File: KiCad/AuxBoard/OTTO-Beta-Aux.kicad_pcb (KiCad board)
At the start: 2 copper layers, 288.5 x 95 mm, 212 parts, among them J1 Conn_01x20, J1_KD028QVFMA17 Conn_02x25_Counter_Clockwise, Q1 AO3400A, SW1 ALPS SKHC, SW10 ALPS SKHC, SW11 ALPS SKHC, SW12 ALPS SKHC, SW13 ALPS SKHC, SW14 ALPS SKHC, SW15 ALPS SKHC, SW16 ALPS SKHC, SW17 ALPS SKHC, SW18 ALPS SKHC, SW19 ALPS SKHC, SW2 ALPS SKHC, SW20 ALPS SKHC, SW21 ALPS SKHC, SW22 ALPS SKHC, SW23 ALPS SKHC, SW24 ALPS SKHC, SW25 ALPS SKHC, SW26 ALPS SKHC, SW27 6x6x13mm, SW28 6x6x13mm, SW29 6x6x13mm, SW3 ALPS SKHC, SW30 6x6x13mm, SW31 6x6x13mm, SW32 6x6x13mm, SW33 6x6x13mm, SW34 6x6x13mm, SW35 6x6x13mm, SW36 6x6x13mm, SW37 6x6x13mm, SW38 6x6x13mm, SW39 6x6x13mm, SW4 ALPS SKHC, SW40 6x6x13mm, SW41 6x6x13mm, SW42 6x6x13mm, SW43 6x6x13mm, SW44 6x6x13mm, SW45 6x6x13mm, SW46 6x6x13mm, SW47 6x6x13mm, SW5 ALPS SKHC, SW50 6x6x13mm, SW51 6x6x13mm, SW52 6x6x13mm, SW53 6x6x13mm, SW54 6x6x13mm, SW55 6x6x13mm, SW56 6x6x13mm, SW6 ALPS SKHC, SW7 ALPS SKHC, SW8 ALPS SKHC, SW9 ALPS SKHC, U1 SN74LV1T34_SOT-23_A, U2 TPS22918_SOT23-6_A

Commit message: Smaller Aux board
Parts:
- removed H3, H4, H5: MountingHole_Pad, OTTO_Footprints_Lib:MountingHoleHole
- removed SW1, SW10, SW11, SW12, SW13, SW14, SW15, SW16, SW2, SW3, SW4, SW5, SW6, SW7, SW8, SW9: ALPS SKHC, OTTO_Footprints_Lib:ALPS_SKHC_aux_hole
- moved FID10 21.2 mm to (153.6, 77.7)
- moved FID4 21.2 mm to (153.6, 77.7)
- moved H102 20.2 mm to (20.2, 86.1)
- moved FID2 14.9 mm to (24.4, 74.2)
- moved FID8 14.9 mm to (24.4, 74.2)
- moved FID12 13.9 mm to (282.2, 80.7)
- moved FID6 13.9 mm to (282.2, 80.7)
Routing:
- net Net-(LED8-Pad2): track 18.7 -> 25.7 mm
- net +5V_LEDS: track 1374.1 -> 1379.5 mm, vias 57 -> 56
- net Net-(LED1-Pad2): track 18.5 -> 16.5 mm
- net GND: vias 119 -> 114
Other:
- board size 288.5 x 95 mm -> 288.5 x 80.1 mm

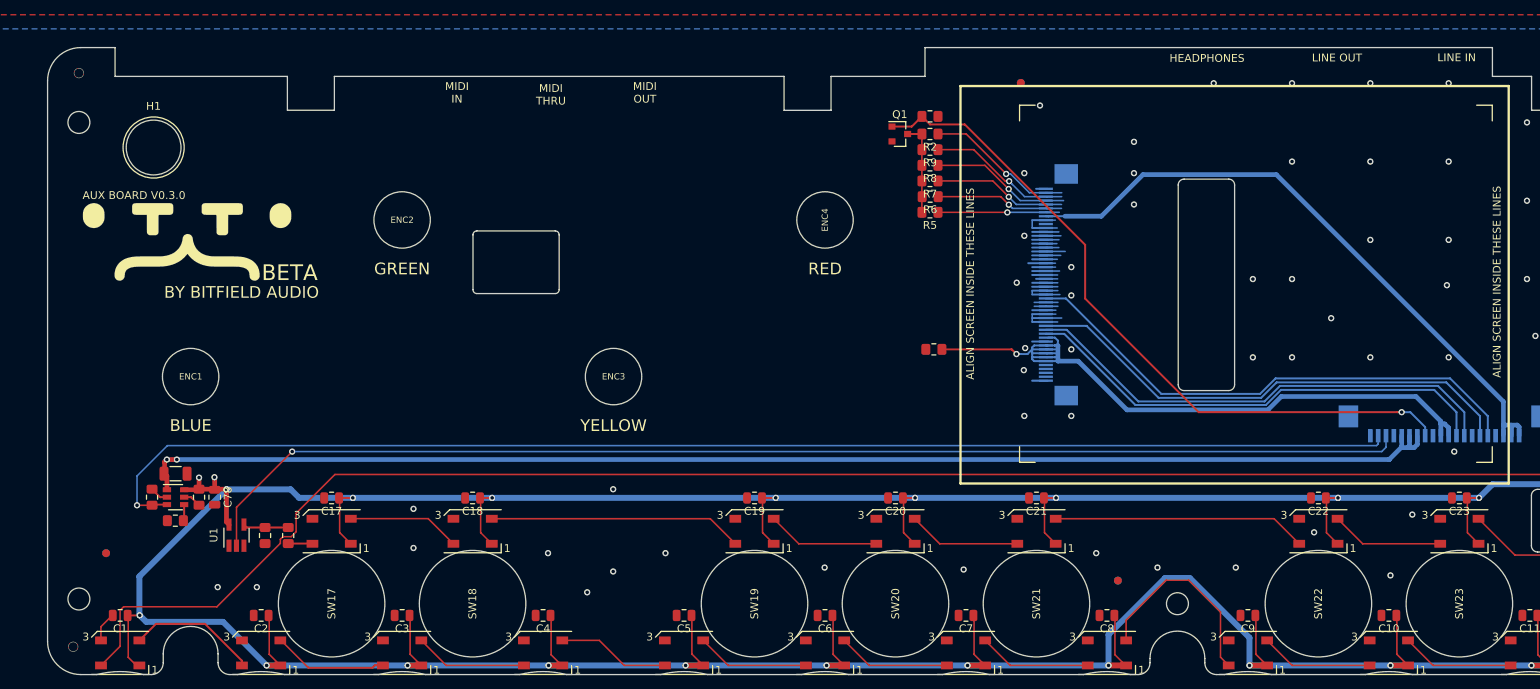
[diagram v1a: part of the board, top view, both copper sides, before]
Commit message: Aux v0.3.0
Small adjustments to PCB outline
switch to WS2812C LEDs
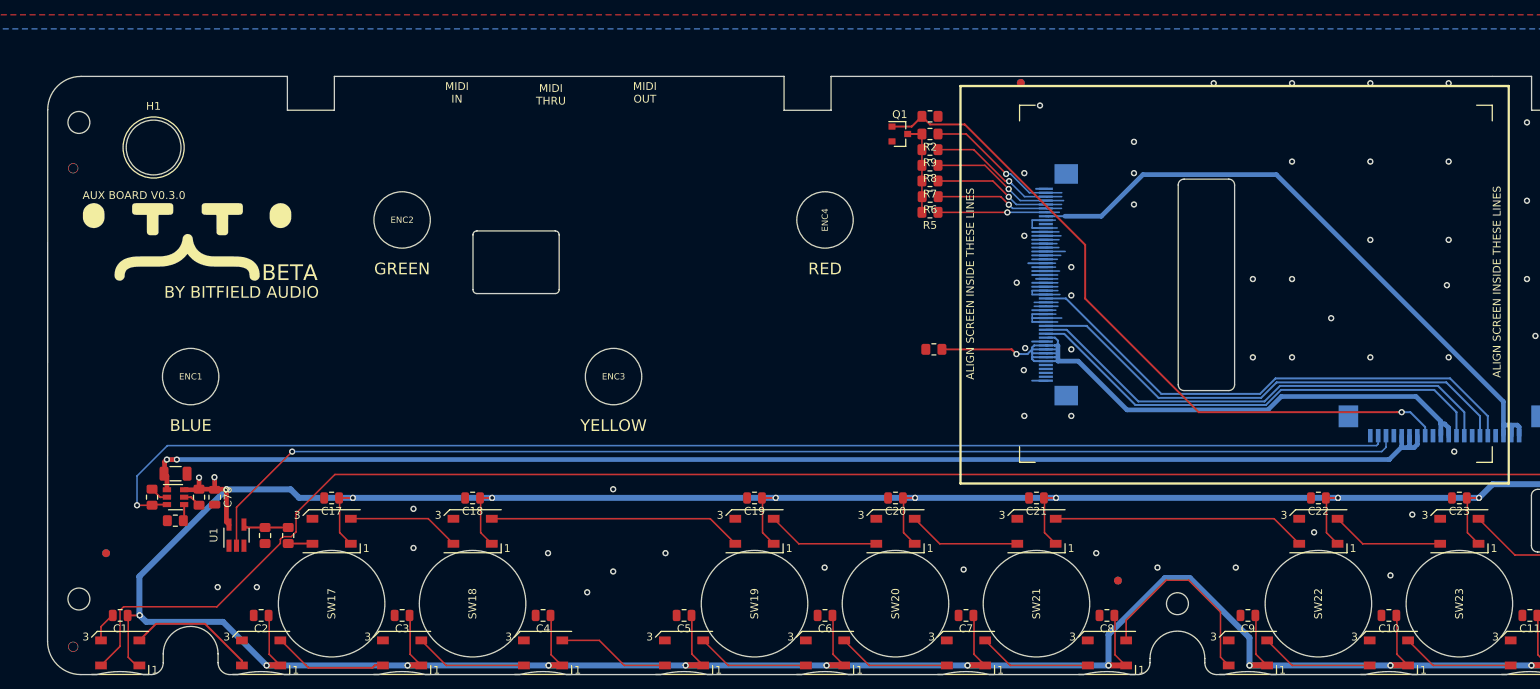
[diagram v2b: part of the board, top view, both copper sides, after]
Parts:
- ENC1, ENC2, ENC3, ENC4: value ALPS EC11E183440C -> ALPS EC11 HOLE
- LED1, LED10, LED11, LED12, LED13, LED14, LED15, LED16, LED17, LED18, LED19, LED2, LED20, LED21, LED22, LED23, LED24, LED25, LED26, LED27, LED28, LED29, LED3, LED30, LED31, LED32, LED33, LED34, LED35, LED36, LED37, LED38, LED39, LED4, LED40, LED41, LED42, LED43, LED44, LED45, LED46, LED47, LED48, LED49, LED5, LED50, LED51, LED52, LED53, LED54, LED6, LED7, LED8, LED9: value WS2812B -> WS2812C
- SW17, SW18, SW19, SW20, SW21, SW22, SW23, SW24, SW25, SW26: value ALPS SKHC -> ALPS SKHC Hole
- SW27, SW28, SW29, SW30, SW31, SW32, SW33, SW34, SW35, SW36, SW37, SW38, SW39, SW40, SW41, SW42, SW43, SW44, SW45, SW46, SW47, SW50, SW51, SW52, SW53, SW54, SW55, SW56: value 6x6x13mm -> 6x6x13mm Hole
- moved H101 12.2 mm to (20.2, 25.0)
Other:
- outline, holes or cut-outs redrawn
- board text removed: "HEADPHONES"
- board text removed: "LINE IN"
- board text removed: "LINE OUT"

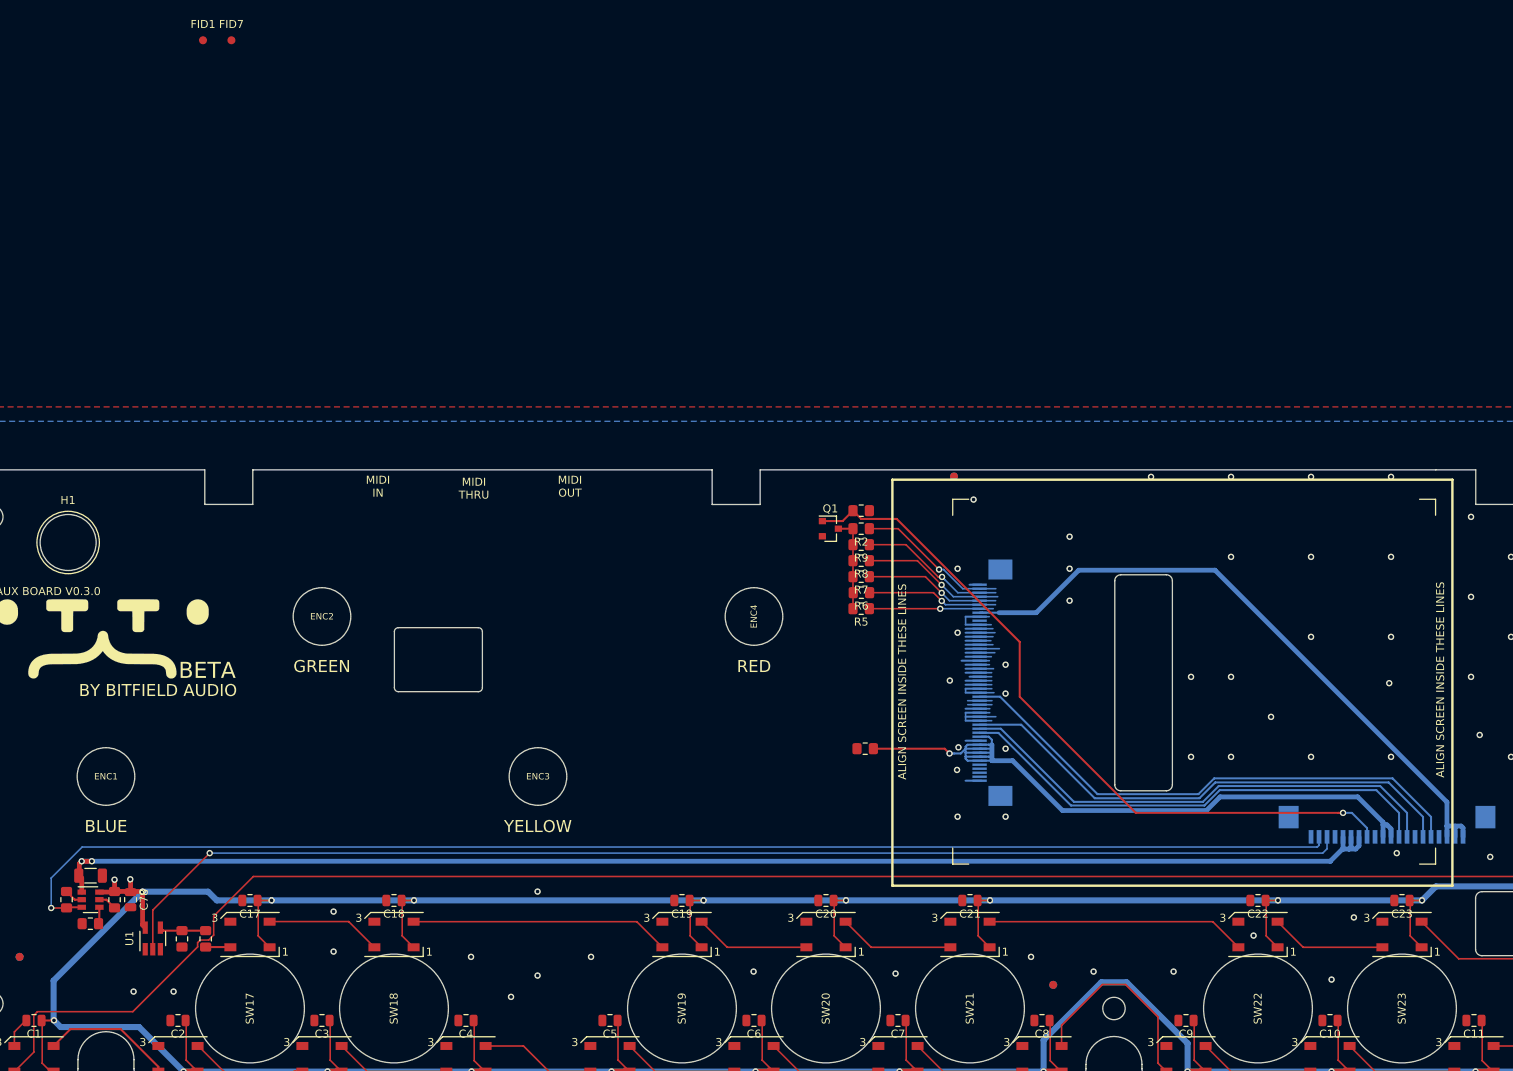
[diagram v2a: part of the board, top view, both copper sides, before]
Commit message: Put LEDs on RPI power rail on aux board
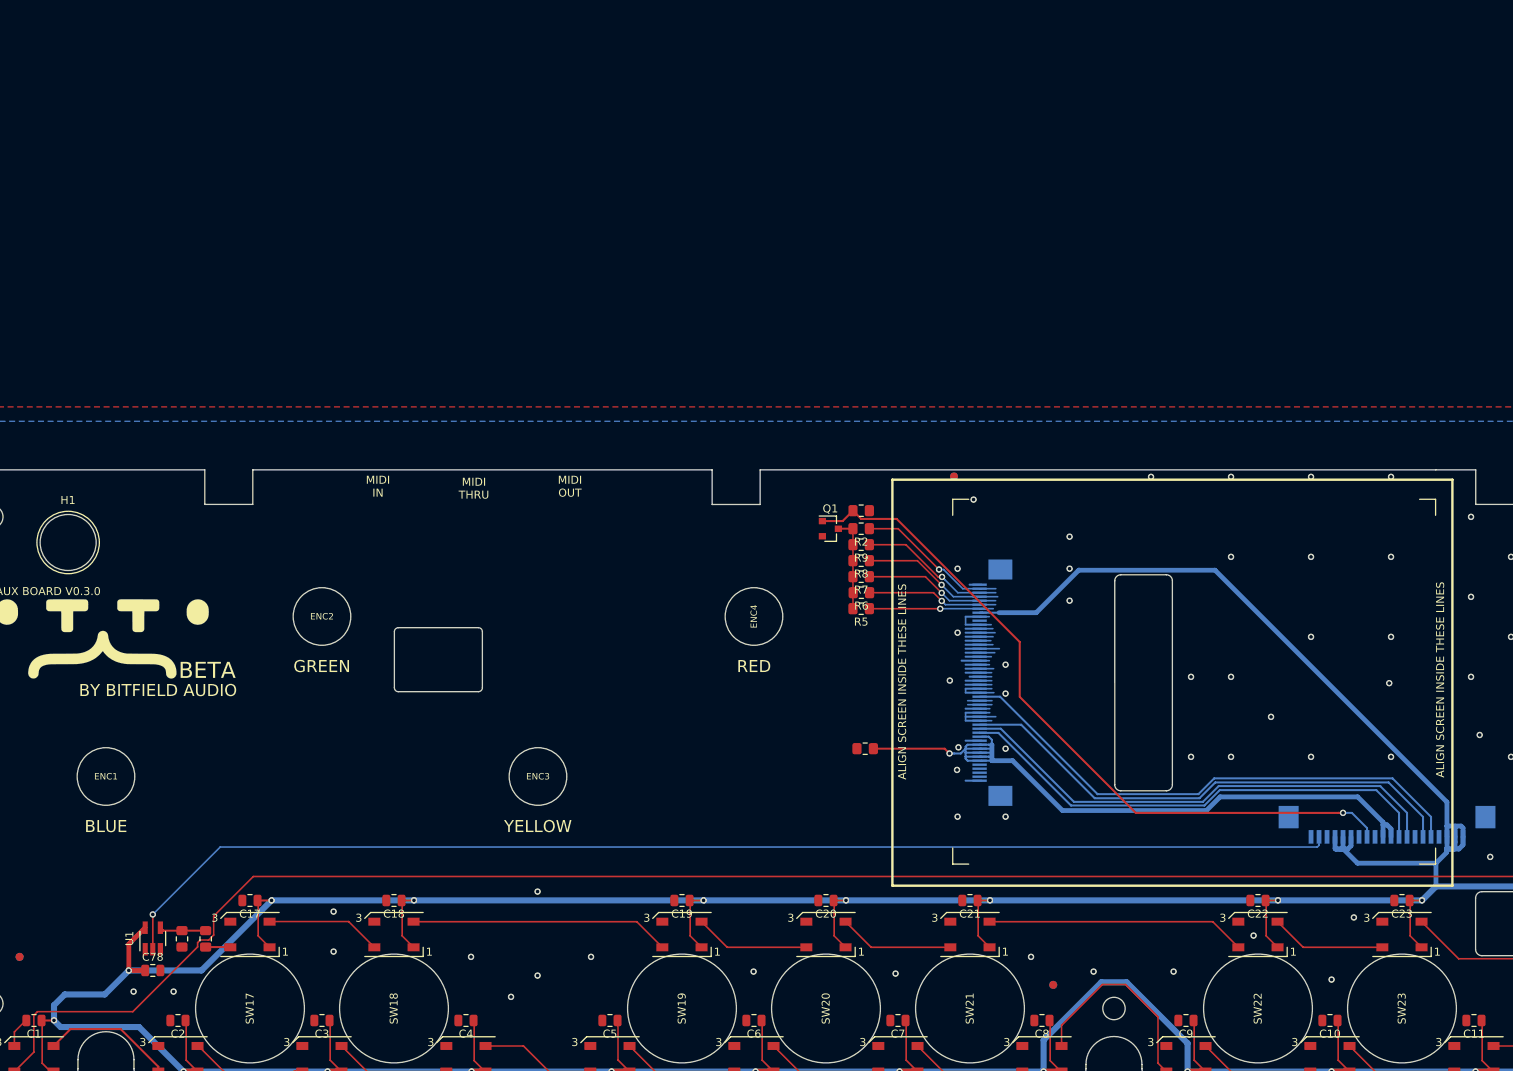
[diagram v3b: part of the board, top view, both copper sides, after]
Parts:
- removed C49: 47uF, Capacitor_SMD:C_1206_3216Metric
- removed C50: 10nF, Capacitor_SMD:C_0805_2012Metric_Pad1.15x1.40mm_HandSolder
- removed FID1, FID7: Fiducial, Fiducial:Fiducial_1mm_Mask2mm
- removed R3: 100k, Resistor_SMD:R_0805_2012Metric_Pad1.15x1.40mm_HandSolder
- removed R4: 0, Resistor_SMD:R_0805_2012Metric_Pad1.15x1.40mm_HandSolder
- removed U2: TPS22918_SOT23-6_A, OTTO_Footprints_Lib:SOT-23-6
- moved C78 9.27 mm to (41.1, 75.8), turned to 0 degrees
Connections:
- C1 pad 1: +5V_LEDS -> +5V
- C10 pad 1: +5V_LEDS -> +5V
- C100 pad 1: +5V_LEDS -> +5V
- C101 pad 1: +5V_LEDS -> +5V
- C102 pad 1: +5V_LEDS -> +5V
- C103 pad 1: +5V_LEDS -> +5V
- C104 pad 1: +5V_LEDS -> +5V
- C105 pad 1: +5V_LEDS -> +5V
- C11 pad 1: +5V_LEDS -> +5V
- C12 pad 1: +5V_LEDS -> +5V
- C13 pad 1: +5V_LEDS -> +5V
- C14 pad 1: +5V_LEDS -> +5V
- C15 pad 1: +5V_LEDS -> +5V
- C16 pad 1: +5V_LEDS -> +5V
- C17 pad 1: +5V_LEDS -> +5V
- C18 pad 1: +5V_LEDS -> +5V
- C19 pad 1: +5V_LEDS -> +5V
- C2 pad 1: +5V_LEDS -> +5V
- C20 pad 1: +5V_LEDS -> +5V
- C21 pad 1: +5V_LEDS -> +5V
- C22 pad 1: +5V_LEDS -> +5V
- C23 pad 1: +5V_LEDS -> +5V
- C24 pad 1: +5V_LEDS -> +5V
- C25 pad 1: +5V_LEDS -> +5V
- C26 pad 1: +5V_LEDS -> +5V
- C27 pad 1: +5V_LEDS -> +5V
- C28 pad 1: +5V_LEDS -> +5V
- C29 pad 1: +5V_LEDS -> +5V
- C3 pad 1: +5V_LEDS -> +5V
- C30 pad 1: +5V_LEDS -> +5V
- C31 pad 1: +5V_LEDS -> +5V
- C32 pad 1: +5V_LEDS -> +5V
- C33 pad 1: +5V_LEDS -> +5V
- C34 pad 1: +5V_LEDS -> +5V
- C35 pad 1: +5V_LEDS -> +5V
- C36 pad 1: +5V_LEDS -> +5V
- C37 pad 1: +5V_LEDS -> +5V
- C38 pad 1: +5V_LEDS -> +5V
- C39 pad 1: +5V_LEDS -> +5V
- C4 pad 1: +5V_LEDS -> +5V
- C40 pad 1: +5V_LEDS -> +5V
- C41 pad 1: +5V_LEDS -> +5V
- C42 pad 1: +5V_LEDS -> +5V
- C43 pad 1: +5V_LEDS -> +5V
- C44 pad 1: +5V_LEDS -> +5V
- C45 pad 1: +5V_LEDS -> +5V
- C46 pad 1: +5V_LEDS -> +5V
- C47 pad 1: +5V_LEDS -> +5V
- C5 pad 1: +5V_LEDS -> +5V
- C6 pad 1: +5V_LEDS -> +5V
- C7 pad 1: +5V_LEDS -> +5V
- C78 pad 1: +5V_LEDS -> +5V
- C8 pad 1: +5V_LEDS -> +5V
- C9 pad 1: +5V_LEDS -> +5V
- C99 pad 1: +5V_LEDS -> +5V
- J1 pad 18: 5V_BACKLIGHT -> +5V
- J1 pad 19: 5V_BACKLIGHT -> +5V
- J1 pad 2: LED_PWR_EN -> /SPI_MOSI_MCU
- J1 pad 20: 5V_BACKLIGHT -> +5V
- J1 pad 3: /SPI_MOSI_MCU -> GND
- J1 pad 4: GND -> +5V
- J1 pad 5: +5V_REG -> +5V
- J1 pad 6: +5V_REG -> +5V
- J1 pad 7: +5V_REG -> GND
- J1_KD028QVFMA17 pad 43: 5V_BACKLIGHT -> +5V
- LED1 pad 1: +5V_LEDS -> +5V
- LED10 pad 1: +5V_LEDS -> +5V
- LED11 pad 1: +5V_LEDS -> +5V
- LED12 pad 1: +5V_LEDS -> +5V
- LED13 pad 1: +5V_LEDS -> +5V
- LED14 pad 1: +5V_LEDS -> +5V
- LED15 pad 1: +5V_LEDS -> +5V
- LED16 pad 1: +5V_LEDS -> +5V
- LED17 pad 1: +5V_LEDS -> +5V
- LED18 pad 1: +5V_LEDS -> +5V
- LED19 pad 1: +5V_LEDS -> +5V
- LED2 pad 1: +5V_LEDS -> +5V
- LED20 pad 1: +5V_LEDS -> +5V
- LED21 pad 1: +5V_LEDS -> +5V
- LED22 pad 1: +5V_LEDS -> +5V
- LED23 pad 1: +5V_LEDS -> +5V
- LED24 pad 1: +5V_LEDS -> +5V
- LED25 pad 1: +5V_LEDS -> +5V
- LED26 pad 1: +5V_LEDS -> +5V
- LED27 pad 1: +5V_LEDS -> +5V
- LED28 pad 1: +5V_LEDS -> +5V
- LED29 pad 1: +5V_LEDS -> +5V
- LED3 pad 1: +5V_LEDS -> +5V
- LED30 pad 1: +5V_LEDS -> +5V
- LED31 pad 1: +5V_LEDS -> +5V
- LED32 pad 1: +5V_LEDS -> +5V
- LED33 pad 1: +5V_LEDS -> +5V
- LED34 pad 1: +5V_LEDS -> +5V
- LED35 pad 1: +5V_LEDS -> +5V
- LED36 pad 1: +5V_LEDS -> +5V
- LED37 pad 1: +5V_LEDS -> +5V
- LED38 pad 1: +5V_LEDS -> +5V
- LED39 pad 1: +5V_LEDS -> +5V
- LED4 pad 1: +5V_LEDS -> +5V
- LED40 pad 1: +5V_LEDS -> +5V
- LED41 pad 1: +5V_LEDS -> +5V
- LED42 pad 1: +5V_LEDS -> +5V
- LED43 pad 1: +5V_LEDS -> +5V
- LED44 pad 1: +5V_LEDS -> +5V
- LED45 pad 1: +5V_LEDS -> +5V
- LED46 pad 1: +5V_LEDS -> +5V
- LED47 pad 1: +5V_LEDS -> +5V
- LED48 pad 1: +5V_LEDS -> +5V
- LED49 pad 1: +5V_LEDS -> +5V
- LED5 pad 1: +5V_LEDS -> +5V
- LED50 pad 1: +5V_LEDS -> +5V
- LED51 pad 1: +5V_LEDS -> +5V
- LED52 pad 1: +5V_LEDS -> +5V
- LED53 pad 1: +5V_LEDS -> +5V
- LED54 pad 1: +5V_LEDS -> +5V
- LED6 pad 1: +5V_LEDS -> +5V
- LED7 pad 1: +5V_LEDS -> +5V
- LED8 pad 1: +5V_LEDS -> +5V
- LED9 pad 1: +5V_LEDS -> +5V
- U1 pad 5: +5V_LEDS -> +5V
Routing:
- net +5V: track 0.00 -> 1488.1 mm, vias 0 -> 54
- net +5V_LEDS: track 1379.5 -> 0.00 mm, vias 56 -> 0
- net +5V_REG: track 170.8 -> 0.00 mm, vias 2 -> 0
- net LED_PWR_EN: track 168.8 -> 0.00 mm, vias 1 -> 0
- net 5V_BACKLIGHT: track 83.2 -> 0.00 mm
- net Net-(R4-Pad2): track 2.32 -> 0.00 mm
- net GND: track 102.7 -> 100.3 mm, vias 114 -> 113
- net Net-(C50-Pad1): track 2.09 -> 0.00 mm
- net /SPI_MOSI_MCU: track 156.3 -> 154.8 mm

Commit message: Redesign for STM32F103
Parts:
- added C49: 47uF, Capacitor_SMD:C_1206_3216Metric, F.Cu at (129.4, 60.5)
- added U2: TPS22918_SOT23-6_A, OTTO_Footprints_Lib:SOT-23-6, F.Cu at (128.1, 63.9)
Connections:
- C1 pad 1: +5V -> +5V_LEDS
- C10 pad 1: +5V -> +5V_LEDS
- C100 pad 1: +5V -> +5V_LEDS
- C101 pad 1: +5V -> +5V_LEDS
- C102 pad 1: +5V -> +5V_LEDS
- C103 pad 1: +5V -> +5V_LEDS
- C104 pad 1: +5V -> +5V_LEDS
- C105 pad 1: +5V -> +5V_LEDS
- C11 pad 1: +5V -> +5V_LEDS
- C12 pad 1: +5V -> +5V_LEDS
- C13 pad 1: +5V -> +5V_LEDS
- C14 pad 1: +5V -> +5V_LEDS
- C15 pad 1: +5V -> +5V_LEDS
- C16 pad 1: +5V -> +5V_LEDS
- C17 pad 1: +5V -> +5V_LEDS
- C18 pad 1: +5V -> +5V_LEDS
- C19 pad 1: +5V -> +5V_LEDS
- C2 pad 1: +5V -> +5V_LEDS
- C20 pad 1: +5V -> +5V_LEDS
- C21 pad 1: +5V -> +5V_LEDS
- C22 pad 1: +5V -> +5V_LEDS
- C23 pad 1: +5V -> +5V_LEDS
- C24 pad 1: +5V -> +5V_LEDS
- C25 pad 1: +5V -> +5V_LEDS
- C26 pad 1: +5V -> +5V_LEDS
- C27 pad 1: +5V -> +5V_LEDS
- C28 pad 1: +5V -> +5V_LEDS
- C29 pad 1: +5V -> +5V_LEDS
- C3 pad 1: +5V -> +5V_LEDS
- C30 pad 1: +5V -> +5V_LEDS
- C31 pad 1: +5V -> +5V_LEDS
- C32 pad 1: +5V -> +5V_LEDS
- C33 pad 1: +5V -> +5V_LEDS
- C34 pad 1: +5V -> +5V_LEDS
- C35 pad 1: +5V -> +5V_LEDS
- C36 pad 1: +5V -> +5V_LEDS
- C37 pad 1: +5V -> +5V_LEDS
- C38 pad 1: +5V -> +5V_LEDS
- C39 pad 1: +5V -> +5V_LEDS
- C4 pad 1: +5V -> +5V_LEDS
- C40 pad 1: +5V -> +5V_LEDS
- C41 pad 1: +5V -> +5V_LEDS
- C42 pad 1: +5V -> +5V_LEDS
- C43 pad 1: +5V -> +5V_LEDS
- C44 pad 1: +5V -> +5V_LEDS
- C45 pad 1: +5V -> +5V_LEDS
- C46 pad 1: +5V -> +5V_LEDS
- C47 pad 1: +5V -> +5V_LEDS
- C5 pad 1: +5V -> +5V_LEDS
- C6 pad 1: +5V -> +5V_LEDS
- C7 pad 1: +5V -> +5V_LEDS
- C78 pad 1: +5V -> +5V_LEDS
- C8 pad 1: +5V -> +5V_LEDS
- C9 pad 1: +5V -> +5V_LEDS
- C99 pad 1: +5V -> +5V_LEDS
- J1 pad 1: GND -> /LED_PWR_EN
- J1 pad 18: +5V -> +5V_RASPI
- J1 pad 19: +5V -> +5V_RASPI
- J1 pad 20: +5V -> +5V_RASPI
- J1 pad 4: +5V -> +5V_REG
- J1 pad 5: +5V -> +5V_REG
- J1 pad 6: +5V -> +5V_REG
- J1_KD028QVFMA17 pad 2: Net-(J1_KD028QVFMA17-Pad2) -> (no net)
- J1_KD028QVFMA17 pad 3: Net-(J1_KD028QVFMA17-Pad3) -> (no net)
- J1_KD028QVFMA17 pad 4: Net-(J1_KD028QVFMA17-Pad4) -> (no net)
- J1_KD028QVFMA17 pad 41: Net-(J1_KD028QVFMA17-Pad41) -> (no net)
- J1_KD028QVFMA17 pad 43: +5V -> +5V_RASPI
- J1_KD028QVFMA17 pad 5: Net-(J1_KD028QVFMA17-Pad5) -> (no net)
- LED1 pad 1: +5V -> +5V_LEDS
- LED10 pad 1: +5V -> +5V_LEDS
- LED11 pad 1: +5V -> +5V_LEDS
- LED12 pad 1: +5V -> +5V_LEDS
- LED13 pad 1: +5V -> +5V_LEDS
- LED14 pad 1: +5V -> +5V_LEDS
- LED15 pad 1: +5V -> +5V_LEDS
- LED16 pad 1: +5V -> +5V_LEDS
- LED17 pad 1: +5V -> +5V_LEDS
- LED18 pad 1: +5V -> +5V_LEDS
- LED19 pad 1: +5V -> +5V_LEDS
- LED2 pad 1: +5V -> +5V_LEDS
- LED20 pad 1: +5V -> +5V_LEDS
- LED21 pad 1: +5V -> +5V_LEDS
- LED22 pad 1: +5V -> +5V_LEDS
- LED23 pad 1: +5V -> +5V_LEDS
- LED24 pad 1: +5V -> +5V_LEDS
- LED25 pad 1: +5V -> +5V_LEDS
- LED26 pad 1: +5V -> +5V_LEDS
- LED27 pad 1: +5V -> +5V_LEDS
- LED28 pad 1: +5V -> +5V_LEDS
- LED29 pad 1: +5V -> +5V_LEDS
- LED3 pad 1: +5V -> +5V_LEDS
- LED30 pad 1: +5V -> +5V_LEDS
- LED31 pad 1: +5V -> +5V_LEDS
- LED32 pad 1: +5V -> +5V_LEDS
- LED33 pad 1: +5V -> +5V_LEDS
- LED34 pad 1: +5V -> +5V_LEDS
- LED35 pad 1: +5V -> +5V_LEDS
- LED36 pad 1: +5V -> +5V_LEDS
- LED37 pad 1: +5V -> +5V_LEDS
- LED38 pad 1: +5V -> +5V_LEDS
- LED39 pad 1: +5V -> +5V_LEDS
- LED4 pad 1: +5V -> +5V_LEDS
- LED40 pad 1: +5V -> +5V_LEDS
- LED41 pad 1: +5V -> +5V_LEDS
- LED42 pad 1: +5V -> +5V_LEDS
- LED43 pad 1: +5V -> +5V_LEDS
- LED44 pad 1: +5V -> +5V_LEDS
- LED45 pad 1: +5V -> +5V_LEDS
- LED46 pad 1: +5V -> +5V_LEDS
- LED47 pad 1: +5V -> +5V_LEDS
- LED48 pad 1: +5V -> +5V_LEDS
- LED49 pad 1: +5V -> +5V_LEDS
- LED5 pad 1: +5V -> +5V_LEDS
- LED50 pad 1: +5V -> +5V_LEDS
- LED51 pad 1: +5V -> +5V_LEDS
- LED52 pad 1: +5V -> +5V_LEDS
- LED53 pad 1: +5V -> +5V_LEDS
- LED54 pad 1: +5V -> +5V_LEDS
- LED54 pad 2: /LEDs/LED_OUT -> (no net)
- LED6 pad 1: +5V -> +5V_LEDS
- LED7 pad 1: +5V -> +5V_LEDS
- LED8 pad 1: +5V -> +5V_LEDS
- LED9 pad 1: +5V -> +5V_LEDS
- U1 pad 1: Net-(U1-Pad1) -> (no net)
- U1 pad 5: +5V -> +5V_LEDS
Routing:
- net +5V: track 1488.1 -> 0.00 mm, vias 54 -> 0
- net +5V_LEDS: track 0.00 -> 1398.8 mm, vias 0 -> 58
- net +5V_RASPI: track 0.00 -> 90.3 mm
- net +5V_REG: track 0.00 -> 71.1 mm, vias 0 -> 1
- net /LED_PWR_EN: track 0.00 -> 63.5 mm, vias 0 -> 1
- net GND: track 100.3 -> 96.6 mm, vias 113 -> 165
- net BL_PWM: track 90.2 -> 92.1 mm
- added copper zone on B.Cu, net +5V_LEDS
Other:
- outline, holes or cut-outs redrawn

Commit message: Version 0.3.0 as ordered
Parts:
- moved FID3 36.3 mm to (105.0, 15.6)
- moved FID9 36.3 mm to (105.0, 15.6)
